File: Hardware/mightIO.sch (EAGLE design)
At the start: 47 parts, among them IC1 TL064D, IC2 TL064D, IC3 LM4041A12DBZ, U1 MAX11612

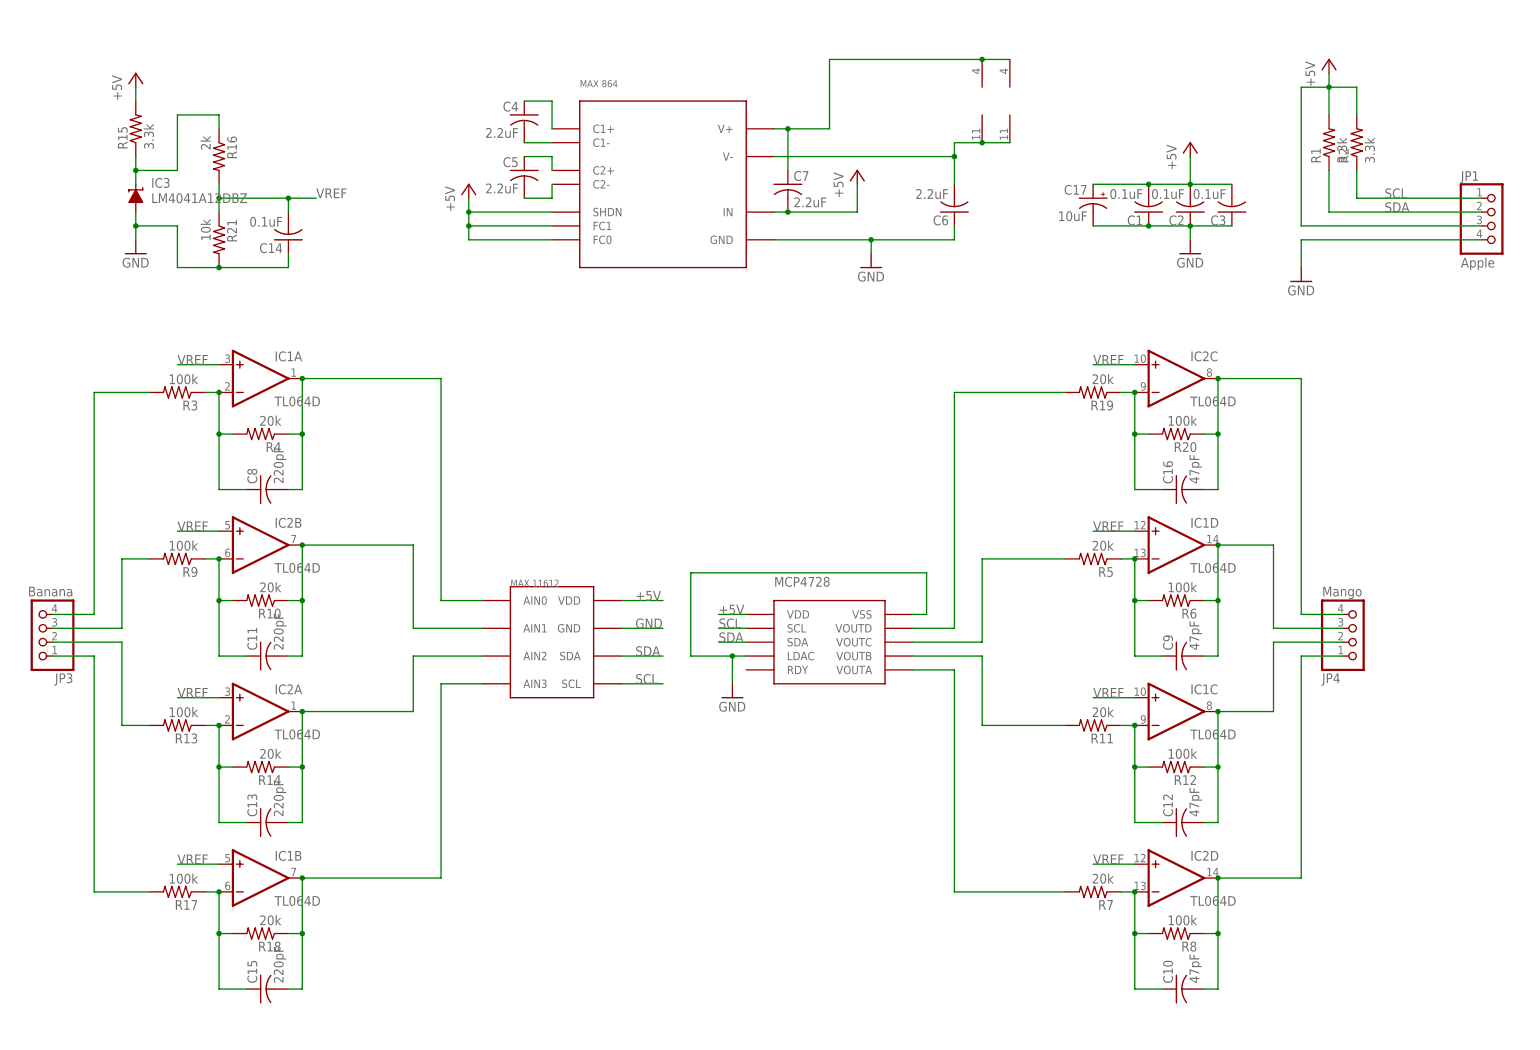
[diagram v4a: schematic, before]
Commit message: Switched output amplifiers to non-inverting
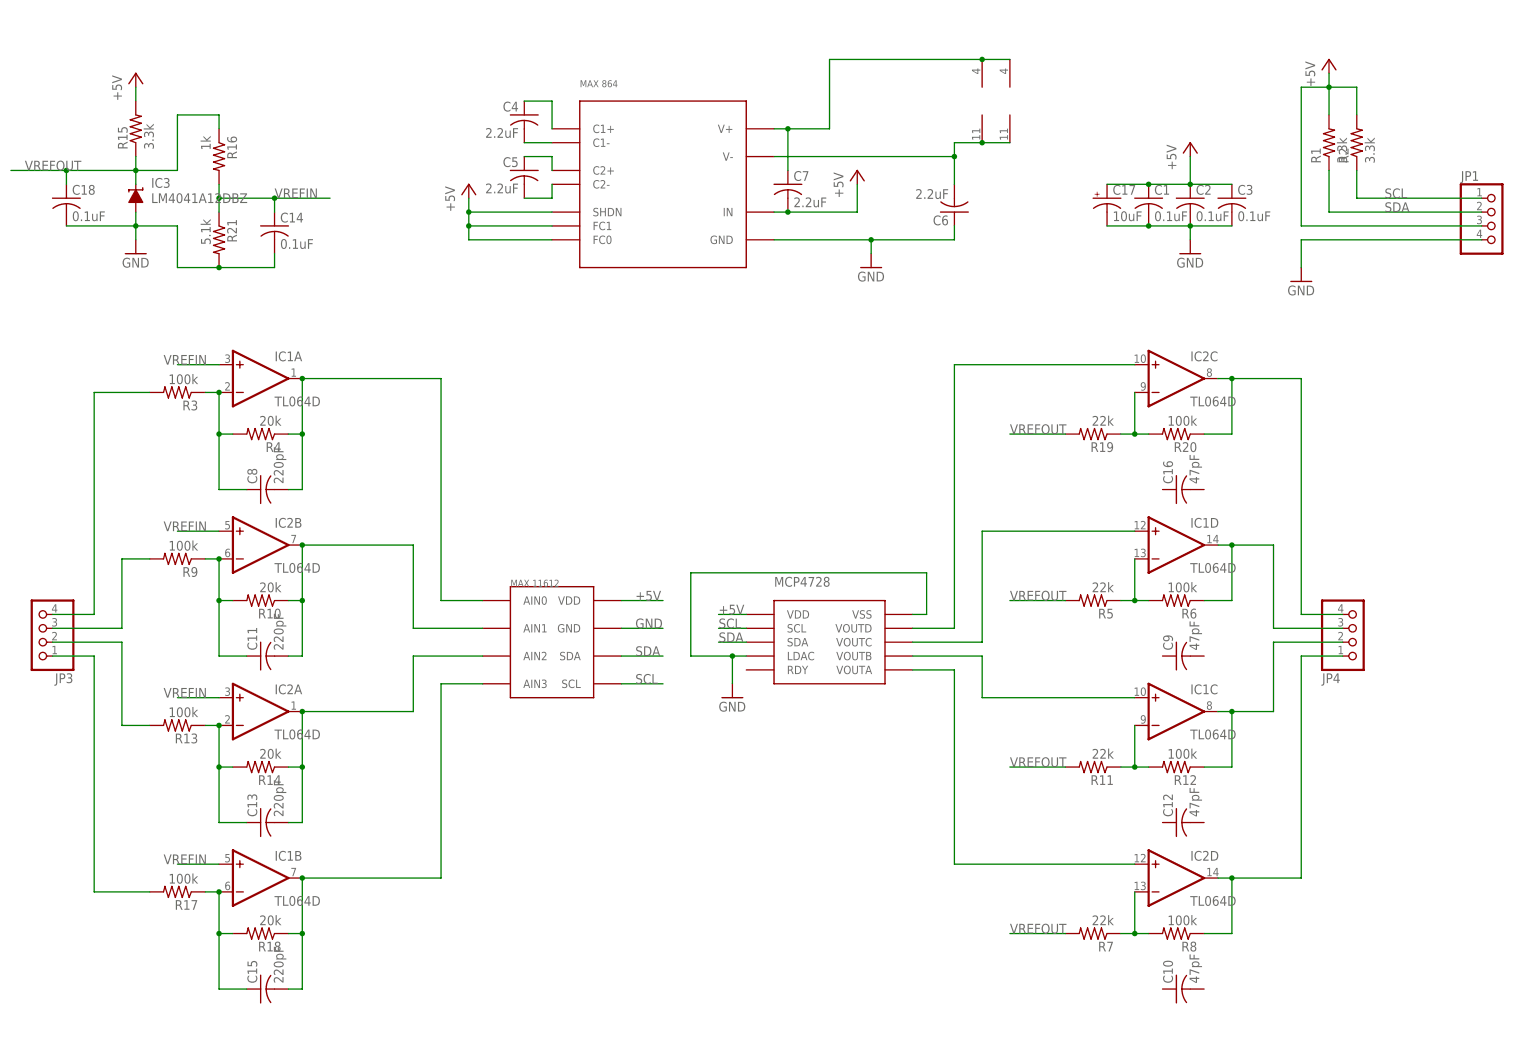
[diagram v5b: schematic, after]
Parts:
- added C18: 0.1uF, rcl:C-USC0603
- JP1: value Apple -> (none)
- JP3: value Banana -> (none)
- JP4: value Mango -> (none)
- R11, R19, R5, R7: value 20k -> 22k
- R16: value 2k -> 1k
- R21: value 10k -> 5.1k
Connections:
- removed net N$15: C9.1, IC1D.-IN, R5.1, R6.2
- removed net N$17: C10.1, IC2D.-IN, R7.1, R8.2
- removed net N$21: C12.1, IC1C.-IN, R11.1, R12.2
- removed net N$26: IC3.C, R15.1, R16.1
- removed net N$29: C16.1, IC2C.-IN, R19.1, R20.2
- removed net VREF: C14.2, IC1A.+IN, IC1B.+IN, IC1C.+IN, IC1D.+IN, IC2A.+IN, IC2B.+IN, IC2C.+IN, IC2D.+IN, R16.2, R21.1
- new net N$2: IC2C.-IN, R19.1, R20.2
- new net N$4: IC1D.-IN, R5.1, R6.2
- new net N$5: IC1C.-IN, R11.1, R12.2
- new net N$6: IC2D.-IN, R7.1, R8.2
- new net VREFIN: C14.1, IC1A.+IN, IC1B.+IN, IC2A.+IN, IC2B.+IN, R16.2, R21.1
- new net VREFOUT: C18.1, IC3.C, R11.2, R15.1, R16.1, R19.2, R5.2, R7.2
- net +5V: now also C1.1, C2.1, C3.1; no longer C1.2, C2.2, C3.2
- net AOA: no longer C10.2
- net AOB: no longer C12.2
- net AOC: no longer C9.2
- net AOD: no longer C16.2
- net GND: now also C1.2, C14.2, C18.2, C2.2, C3.2; no longer C1.1, C14.1, C2.1, C3.1
- net N$1: now also IC2C.+IN; no longer R19.2
- net N$25: now also IC2D.+IN; no longer R7.2
- net N$3: now also IC1C.+IN; no longer R11.2
- net N$34: now also IC1D.+IN; no longer R5.2
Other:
- moved on the sheet: C1, C14, C17, C2, C3, R11, R19, R5, R7

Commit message: Touched up silkscreen, moved caps
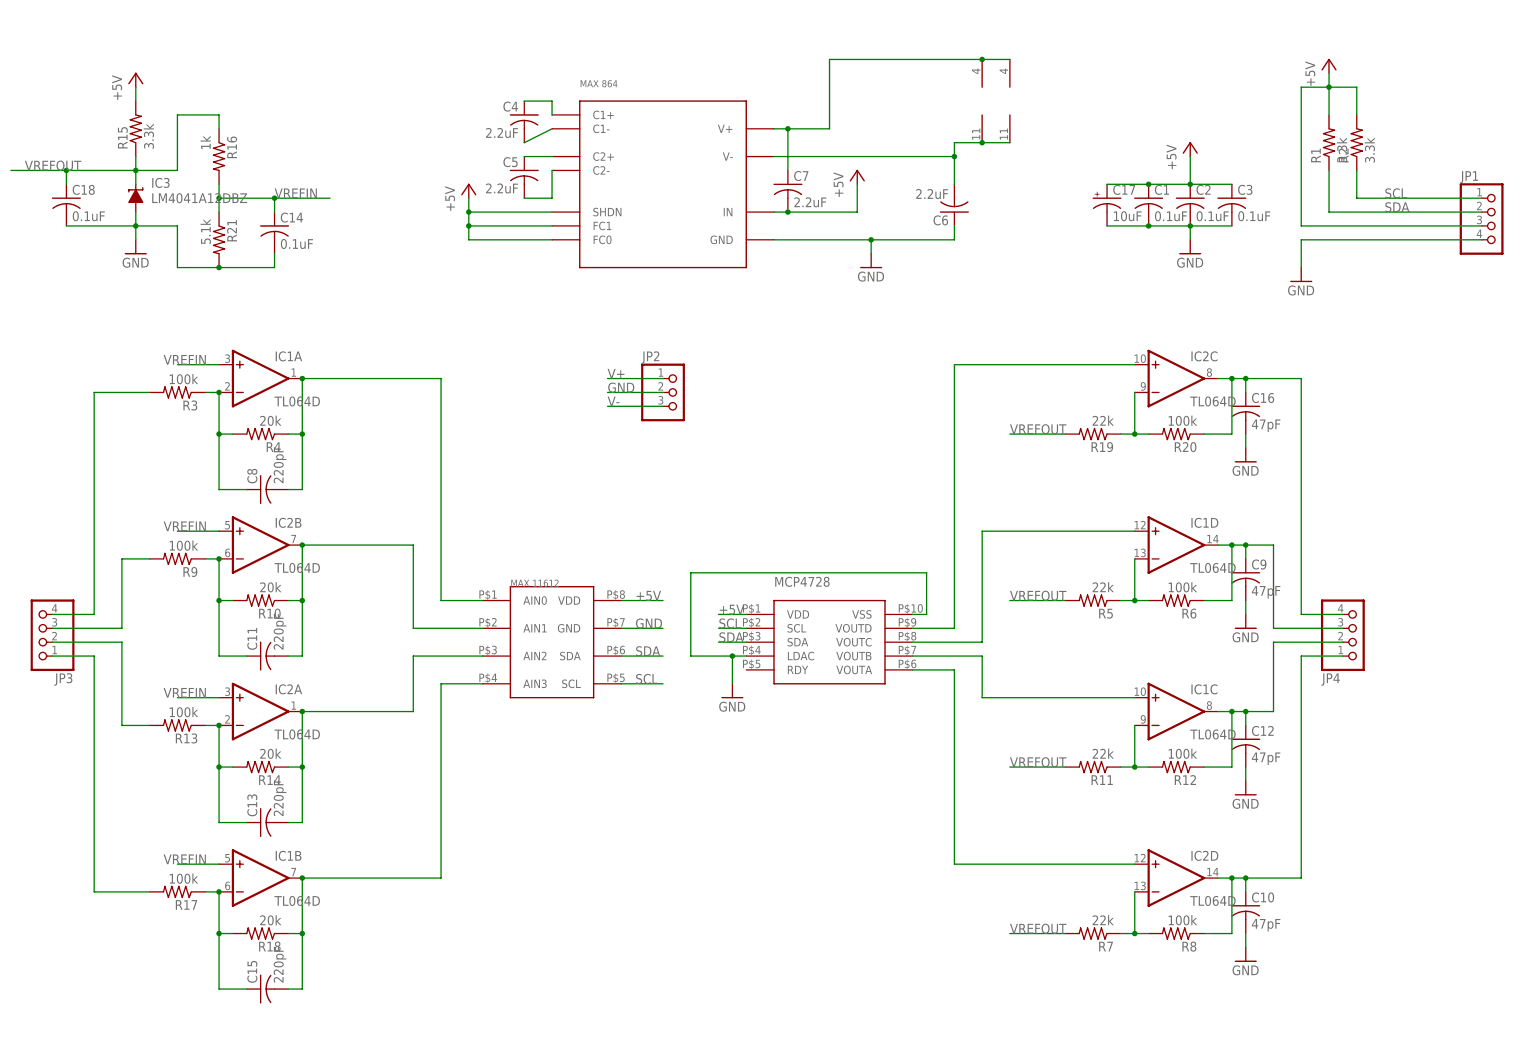
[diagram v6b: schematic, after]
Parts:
- added JP2: (no value), pinhead:PINHD-1X3
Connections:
- net AOA: now also C10.1
- net AOB: now also C12.1
- net AOC: now also C9.1
- net AOD: now also C16.1
- net GND: now also C10.2, C12.2, C16.2, C9.2, JP2.2
- net V+: now also JP2.1
- net V-: now also JP2.3
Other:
- moved on the sheet: C10, C12, C16, C9
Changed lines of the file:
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@@
 <part name="C17" library="rcl" deviceset="CPOL-US" device="E2.5-6" value="10uF"/>
 <part name="C18" library="rcl" deviceset="C-US" device="C0603" value="0.1uF"/>
+<part name="GND6" library="supply1" deviceset="GND" device=""/>
+<part name="GND7" library="supply1" deviceset="GND" device=""/>
+<part name="GND8" library="supply1" deviceset="GND" device=""/>
+<part name="GND9" library="supply1" deviceset="GND" device=""/>
+<part name="JP2" library="pinhead" deviceset="PINHD-1X3" device=""/>
 </parts>
 <sheets>
@@
 <instance part="R5" gate="G$1" x="111.76" y="-2.54" rot="R180"/>
 <instance part="R6" gate="G$1" x="127" y="-2.54" rot="R180"/>
-<instance part="C9" gate="G$1" x="127" y="-12.7" rot="R90"/>
+<instance part="C9" gate="G$1" x="139.7" y="2.54"/>
 <instance part="R7" gate="G$1" x="111.76" y="-63.5" rot="R180"/>
 <instance part="R8" gate="G$1" x="127" y="-63.5" rot="R180"/>
-<instance part="C10" gate="G$1" x="127" y="-73.66" rot="R90"/>
+<instance part="C10" gate="G$1" x="139.7" y="-58.42"/>
 <instance part="R9" gate="G$1" x="-55.88" y="5.08" rot="R180"/>
 <instance part="R10" gate="G$1" x="-40.64" y="-2.54" rot="R180"/>
@@
 <instance part="R11" gate="G$1" x="111.76" y="-33.02" rot="R180"/>
 <instance part="R12" gate="G$1" x="127" y="-33.02" rot="R180"/>
-<instance part="C12" gate="G$1" x="127" y="-43.18" rot="R90"/>
+<instance part="C12" gate="G$1" x="139.7" y="-27.94"/>
 <instance part="R13" gate="G$1" x="-55.88" y="-25.4" rot="R180"/>
 <instance part="R14" gate="G$1" x="-40.64" y="-33.02" rot="R180"/>
@@
 <instance part="R19" gate="G$1" x="111.76" y="27.94" rot="R180"/>
 <instance part="R20" gate="G$1" x="127" y="27.94" rot="R180"/>
-<instance part="C16" gate="G$1" x="127" y="17.78" rot="R90"/>
+<instance part="C16" gate="G$1" x="139.7" y="33.02"/>
 <instance part="IC3" gate="G$1" x="-63.5" y="71.12"/>
 <instance part="R15" gate="G$1" x="-63.5" y="83.82" rot="R90"/>
@@
 <instance part="C17" gate="G$1" x="114.3" y="71.12"/>
 <instance part="C18" gate="G$1" x="-76.2" y="71.12"/>
+<instance part="GND6" gate="1" x="139.7" y="22.86"/>
+<instance part="GND7" gate="1" x="139.7" y="-7.62"/>
+<instance part="GND8" gate="1" x="139.7" y="-38.1"/>
+<instance part="GND9" gate="1" x="139.7" y="-68.58"/>
+<instance part="JP2" gate="A" x="35.56" y="35.56"/>
 </instances>
 <busses>
@@
 <wire x1="129.54" y1="66.04" x2="137.16" y2="66.04" width="0.1524" layer="91"/>
 </segment>
+<segment>
+<pinref part="GND6" gate="1" pin="GND"/>
+<pinref part="C16" gate="G$1" pin="2"/>
+<wire x1="139.7" y1="25.4" x2="139.7" y2="27.94" width="0.1524" layer="91"/>
+</segment>
+<segment>
+<pinref part="GND7" gate="1" pin="GND"/>
+<pinref part="C9" gate="G$1" pin="2"/>
+<wire x1="139.7" y1="-5.08" x2="139.7" y2="-2.54" width="0.1524" layer="91"/>
+</segment>
+<segment>
+<pinref part="GND8" gate="1" pin="GND"/>
+<pinref part="C12" gate="G$1" pin="2"/>
+<wire x1="139.7" y1="-35.56" x2="139.7" y2="-33.02" width="0.1524" layer="91"/>
+</segment>
+<segment>
+<pinref part="GND9" gate="1" pin="GND"/>
+<pinref part="C10" gate="G$1" pin="2"/>
+<wire x1="139.7" y1="-66.04" x2="139.7" y2="-63.5" width="0.1524" layer="91"/>
+</segment>
+<segment>
+<pinref part="JP2" gate="A" pin="2"/>
+<wire x1="33.02" y1="35.56" x2="22.86" y2="35.56" width="0.1524" layer="91"/>
+<label x="22.86" y="35.56" size="1.778" layer="95"/>
+</segment>
 </net>
 <net name="+5V" class="1">
@@
 <pinref part="U$1" gate="G$1" pin="C1+"/>
 <wire x1="7.62" y1="88.9" x2="12.7" y2="88.9" width="0.1524" layer="91"/>
-<wire x1="12.7" y1="88.9" x2="12.7" y2="83.82" width="0.1524" layer="91"/>
+<wire x1="12.7" y1="88.9" x2="12.7" y2="86.36" width="0.1524" layer="91"/>
 </segment>
 </net>
@@
 <pinref part="C4" gate="G$1" pin="2"/>
 <pinref part="U$1" gate="G$1" pin="C1-"/>
-<wire x1="7.62" y1="81.28" x2="12.7" y2="81.28" width="0.1524" layer="91"/>
+<wire x1="7.62" y1="81.28" x2="12.7" y2="83.82" width="0.1524" layer="91"/>
 </segment>
 </net>
@@
 <pinref part="U$1" gate="G$1" pin="C2+"/>
 <wire x1="7.62" y1="78.74" x2="12.7" y2="78.74" width="0.1524" layer="91"/>
-<wire x1="12.7" y1="78.74" x2="12.7" y2="76.2" width="0.1524" layer="91"/>
 </segment>
 </net>
@@
 <pinref part="U$1" gate="G$1" pin="C2-"/>
 <wire x1="7.62" y1="71.12" x2="12.7" y2="71.12" width="0.1524" layer="91"/>
-<wire x1="12.7" y1="71.12" x2="12.7" y2="73.66" width="0.1524" layer="91"/>
+<wire x1="12.7" y1="71.12" x2="12.7" y2="76.2" width="0.1524" layer="91"/>
 </segment>
 </net>
@@
 <junction x="91.44" y="96.52"/>
 </segment>
+<segment>
+<pinref part="JP2" gate="A" pin="1"/>
+<wire x1="33.02" y1="38.1" x2="22.86" y2="38.1" width="0.1524" layer="91"/>
+<label x="22.86" y="38.1" size="1.778" layer="95"/>
+</segment>
 </net>
 <net name="N$11" class="0">
@@
 <junction x="86.36" y="78.74"/>
 </segment>
+<segment>
+<pinref part="JP2" gate="A" pin="3"/>
+<wire x1="33.02" y1="33.02" x2="22.86" y2="33.02" width="0.1524" layer="91"/>
+<label x="22.86" y="33.02" size="1.778" layer="95"/>
+</segment>
 </net>
 <net name="AI1" class="0">
@@
 <pinref part="IC2" gate="D" pin="OUT"/>
 <wire x1="134.62" y1="-53.34" x2="137.16" y2="-53.34" width="0.1524" layer="91"/>
-<wire x1="137.16" y1="-53.34" x2="149.86" y2="-53.34" width="0.1524" layer="91"/>
+<wire x1="137.16" y1="-53.34" x2="139.7" y2="-53.34" width="0.1524" layer="91"/>
+<wire x1="139.7" y1="-53.34" x2="149.86" y2="-53.34" width="0.1524" layer="91"/>
 <wire x1="149.86" y1="-53.34" x2="149.86" y2="-12.7" width="0.1524" layer="91"/>
 <pinref part="JP4" gate="A" pin="1"/>
@@
 <wire x1="137.16" y1="-63.5" x2="137.16" y2="-53.34" width="0.1524" layer="91"/>
 <junction x="137.16" y="-53.34"/>
+<pinref part="C10" gate="G$1" pin="1"/>
+<wire x1="139.7" y1="-55.88" x2="139.7" y2="-53.34" width="0.1524" layer="91"/>
+<junction x="139.7" y="-53.34"/>
 </segment>
 </net>
@@
 <pinref part="IC1" gate="D" pin="OUT"/>
 <wire x1="134.62" y1="7.62" x2="137.16" y2="7.62" width="0.1524" layer="91"/>
-<wire x1="137.16" y1="7.62" x2="144.78" y2="7.62" width="0.1524" layer="91"/>
+<wire x1="137.16" y1="7.62" x2="139.7" y2="7.62" width="0.1524" layer="91"/>
+<wire x1="139.7" y1="7.62" x2="144.78" y2="7.62" width="0.1524" layer="91"/>
 <wire x1="144.78" y1="7.62" x2="144.78" y2="-7.62" width="0.1524" layer="91"/>
 <pinref part="JP4" gate="A" pin="3"/>
@@
 <wire x1="137.16" y1="-2.54" x2="137.16" y2="7.62" width="0.1524" layer="91"/>
 <junction x="137.16" y="7.62"/>
+<pinref part="C9" gate="G$1" pin="1"/>
+<wire x1="139.7" y1="5.08" x2="139.7" y2="7.62" width="0.1524" layer="91"/>
+<junction x="139.7" y="7.62"/>
 </segment>
 </net>
@@
 <pinref part="IC2" gate="C" pin="OUT"/>
 <wire x1="134.62" y1="38.1" x2="137.16" y2="38.1" width="0.1524" layer="91"/>
-<wire x1="137.16" y1="38.1" x2="149.86" y2="38.1" width="0.1524" layer="91"/>
+<wire x1="137.16" y1="38.1" x2="139.7" y2="38.1" width="0.1524" layer="91"/>
+<wire x1="139.7" y1="38.1" x2="149.86" y2="38.1" width="0.1524" layer="91"/>
 <wire x1="149.86" y1="38.1" x2="149.86" y2="-5.08" width="0.1524" layer="91"/>
 <pinref part="JP4" gate="A" pin="4"/>
@@
 <wire x1="137.16" y1="27.94" x2="137.16" y2="38.1" width="0.1524" layer="91"/>
 <junction x="137.16" y="38.1"/>
+<pinref part="C16" gate="G$1" pin="1"/>
+<wire x1="139.7" y1="35.56" x2="139.7" y2="38.1" width="0.1524" layer="91"/>
+<junction x="139.7" y="38.1"/>
 </segment>
 </net>
@@
 <pinref part="IC1" gate="C" pin="OUT"/>
 <wire x1="134.62" y1="-22.86" x2="137.16" y2="-22.86" width="0.1524" layer="91"/>
-<wire x1="137.16" y1="-22.86" x2="144.78" y2="-22.86" width="0.1524" layer="91"/>
+<wire x1="137.16" y1="-22.86" x2="139.7" y2="-22.86" width="0.1524" layer="91"/>
+<wire x1="139.7" y1="-22.86" x2="144.78" y2="-22.86" width="0.1524" layer="91"/>
 <wire x1="144.78" y1="-22.86" x2="144.78" y2="-10.16" width="0.1524" layer="91"/>
 <pinref part="JP4" gate="A" pin="2"/>
@@
 <wire x1="137.16" y1="-33.02" x2="137.16" y2="-22.86" width="0.1524" layer="91"/>
 <junction x="137.16" y="-22.86"/>
-</segment>
-</net>
+<pinref part="C12" gate="G$1" pin="1"/>
+<wire x1="139.7" y1="-25.4" x2="139.7" y2="-22.86" width="0.1524" layer="91"/>
+<junction x="139.7" y="-22.86"/>
+</segment>
+</net>

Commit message: Fixed up previous bugs in offsets
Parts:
- R21: value 5.1k -> 2k
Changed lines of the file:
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@@
 <?xml version="1.0" encoding="utf-8"?>
 <!DOCTYPE eagle SYSTEM "eagle.dtd">
-<eagle version="7.0.0">
+<eagle version="6.5.0">
 <drawing>
 <settings>
@@
 <part name="R15" library="rcl" deviceset="R-US_" device="R0603" value="3.3k"/>
 <part name="R16" library="rcl" deviceset="R-US_" device="R0603" value="1k"/>
-<part name="R21" library="rcl" deviceset="R-US_" device="R0603" value="5.1k"/>
+<part name="R21" library="rcl" deviceset="R-US_" device="R0603" value="2k"/>
 <part name="P+5" library="supply1" deviceset="+5V" device=""/>
 <part name="GND4" library="supply1" deviceset="GND" device=""/>

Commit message: Annotated schematic and labeled board
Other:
- note added: "Arduino header"
- note added: "Input header"
- note added: "Input opamp downscaling"
- note added: "Op-amp supply rails"
- note added: "Output header"
- note added: "Output opamp upscaling"
- note added: "Power supply caps"
- note added: "Reference voltages"
- note added: "Split rail breakout"
- note added: "mightIO v1.0 Tamas Szalay"
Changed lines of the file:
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@@
 <sheet>
 <plain>
+<text x="154.94" y="2.54" size="2.54" layer="97">Output
+header</text>
+<text x="-86.36" y="5.08" size="2.54" layer="97">Input
+header</text>
+<text x="-73.66" y="99.06" size="2.54" layer="97">Reference voltages</text>
+<text x="-78.74" y="-76.2" size="2.54" layer="97">Input opamp
+downscaling</text>
+<text x="109.22" y="-81.28" size="2.54" layer="97">Output opamp
+upscaling</text>
+<text x="160.02" y="53.34" size="2.54" layer="97">Arduino header</text>
+<text x="109.22" y="86.36" size="2.54" layer="97">Power supply caps</text>
+<text x="58.42" y="101.6" size="2.54" layer="97">Op-amp supply rails</text>
+<text x="22.86" y="-40.64" size="2.54" layer="97">mightIO v1.0
+Tamas Szalay</text>
+<text x="22.86" y="20.32" size="2.54" layer="97">Split rail
+breakout</text>
 </plain>
 <instances>
@@
 </schematic>
 </drawing>
+<compatibility>
+<note version="6.3" minversion="6.2.2" severity="warning">
+Since Version 6.2.2 text objects can contain more than one line,
+which will not be processed correctly with this version.
+</note>
+</compatibility>
 </eagle>
